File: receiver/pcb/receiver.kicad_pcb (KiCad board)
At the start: 2 copper layers, 39 x 43.2 mm, 23 parts, among them M1 Conn_01x02_Female, M2 Conn_01x02_Female, U1 DRV8870DDA, U2 DRV8870DDA

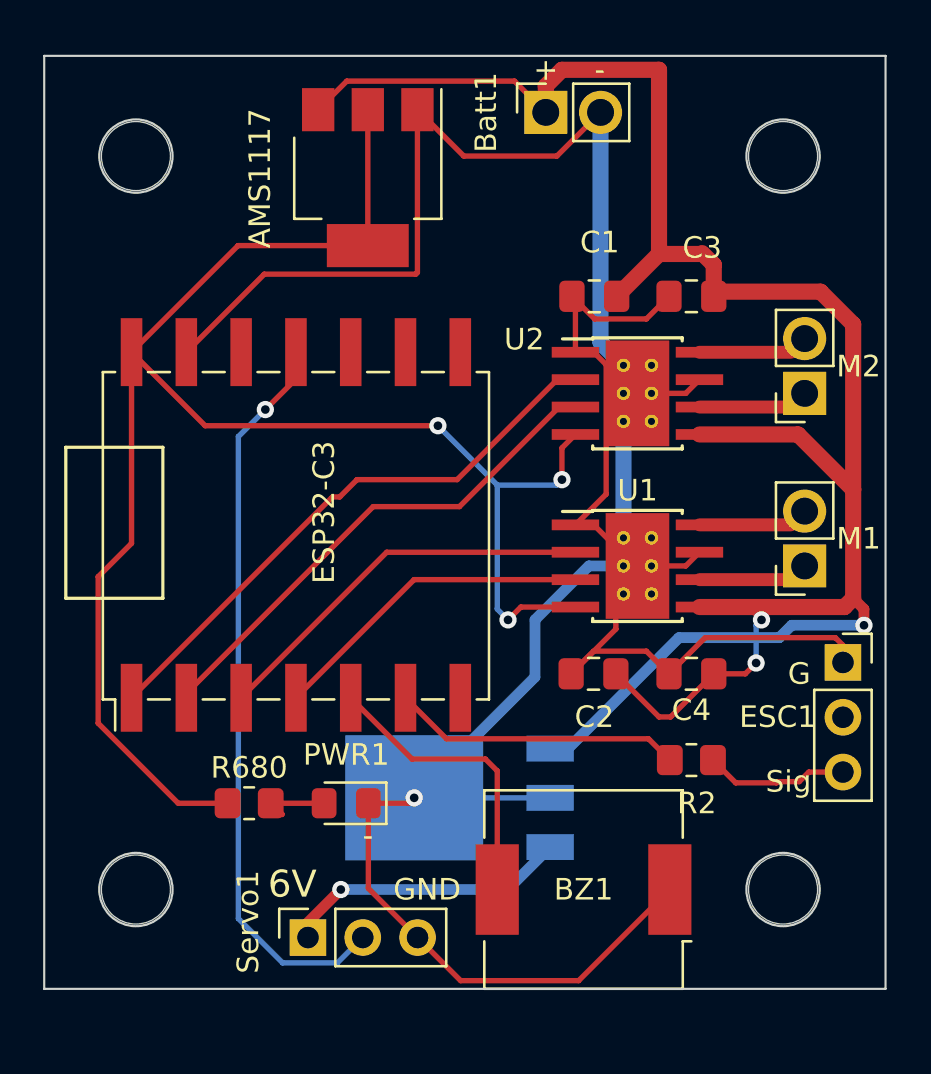
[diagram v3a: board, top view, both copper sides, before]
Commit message: made square pin consistently more positive voltage
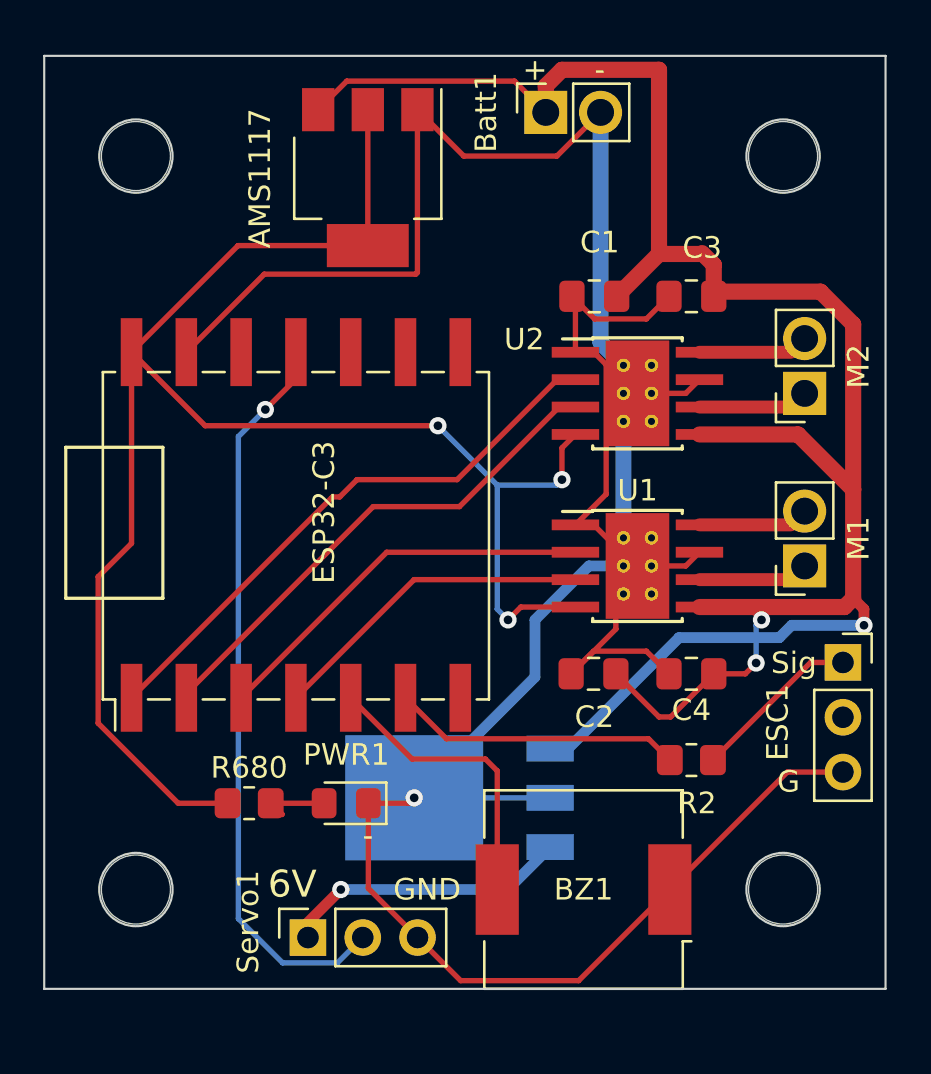
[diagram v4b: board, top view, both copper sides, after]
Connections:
- ESC1 pad 1: GND -> Net-(ESC1-Pad1)
- ESC1 pad 3: Net-(R2-Pad2) -> GND
- R2 pad 2: Net-(R2-Pad2) -> Net-(ESC1-Pad1)
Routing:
- net Net-(ESC1-Pad1): track 0.00 -> 7.90 mm
- net Net-(R2-Pad2): track 6.67 -> 0.00 mm
- net GND: track 140.7 -> 141.3 mm
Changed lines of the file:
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@@
   (net 6 "Net-(M2-Pad1)")
   (net 7 "Net-(M2-Pad2)")
-  (net 8 "Net-(R2-Pad2)")
+  (net 8 "Net-(ESC1-Pad1)")
   (net 9 "Net-(ESP32-C3-Pad19)")
-  (net 10 "Net-(U1-Pad2)")
-  (net 11 "Net-(U1-Pad3)")
+  (net 10 "Net-(ESP32-C3-Pad5)")
+  (net 11 "Net-(ESP32-C3-Pad6)")
   (net 12 "+3V3")
-  (net 13 "Net-(U2-Pad2)")
-  (net 14 "Net-(U2-Pad3)")
+  (net 13 "Net-(ESP32-C3-Pad12)")
+  (net 14 "Net-(ESP32-C3-Pad13)")
   (net 15 "unconnected-(ESP32-C3-Pad20)")
   (net 16 "/spkr")
@@
       (net 12 "+3V3") (pinfunction "3V3") (pintype "power_in"))
     (pad "5" smd rect (at -8.6 -4.34 90) (size 3.15 1) (layers "F.Cu" "F.Paste" "F.Mask")
-      (net 10 "Net-(U1-Pad2)") (pinfunction "GPIO2/ADC1_CH2") (pintype "bidirectional"))
+      (net 10 "Net-(ESP32-C3-Pad5)") (pinfunction "GPIO2/ADC1_CH2") (pintype "bidirectional"))
     (pad "6" smd rect (at -8.6 -1.8 90) (size 3.15 1) (layers "F.Cu" "F.Paste" "F.Mask")
-      (net 11 "Net-(U1-Pad3)") (pinfunction "GPIO3/ADC1_CH3") (pintype "bidirectional"))
+      (net 11 "Net-(ESP32-C3-Pad6)") (pinfunction "GPIO3/ADC1_CH3") (pintype "bidirectional"))
     (pad "12" smd rect (at -8.6 -9.42 90) (size 3.15 1) (layers "F.Cu" "F.Paste" "F.Mask")
-      (net 13 "Net-(U2-Pad2)") (pinfunction "GPIO0/ADC1_CH0/XTAL_32K_P") (pintype "bidirectional"))
+      (net 13 "Net-(ESP32-C3-Pad12)") (pinfunction "GPIO0/ADC1_CH0/XTAL_32K_P") (pintype "bidirectional"))
     (pad "13" smd rect (at -8.6 -6.88 90) (size 3.15 1) (layers "F.Cu" "F.Paste" "F.Mask")
-      (net 14 "Net-(U2-Pad3)") (pinfunction "GPIO1/ADC1_CH1/XTAL_32K_N") (pintype "bidirectional"))
+      (net 14 "Net-(ESP32-C3-Pad13)") (pinfunction "GPIO1/ADC1_CH1/XTAL_32K_N") (pintype "bidirectional"))
     (pad "16" smd rect (at 7.425 -1.8 90) (size 3.15 1) (layers "F.Cu" "F.Paste" "F.Mask")
       (net 19 "/Servo") (pinfunction "GPIO10") (pintype "bidirectional"))
@@
       (net 9 "Net-(ESP32-C3-Pad19)") (pintype "passive"))
     (pad "2" smd roundrect (at 1 0) (size 1.2 1.4) (layers "F.Cu" "F.Paste" "F.Mask") (roundrect_rratio 0.2083333333)
-      (net 8 "Net-(R2-Pad2)") (pintype "passive"))
+      (net 8 "Net-(ESC1-Pad1)") (pintype "passive"))
     (model "${KICAD6_3DMODEL_DIR}/Resistor_SMD.3dshapes/R_0805_2012Metric.wrl"
       (offset (xyz 0 0 0))
@@
     (property "Sheetname" "")
     (attr through_hole)
-    (fp_text reference "ESC1" (at -3.025 2.525) (layer "F.SilkS")
+    (fp_text reference "ESC1" (at -3.025 2.775 90) (layer "F.SilkS")
       (effects (font (size 1 1) (thickness 0.15)))
     )
@@
     (fp_line (start -1.27 6.35) (end -1.27 -1.27) (layer "F.Fab") (width 0.1))
     (pad "1" thru_hole rect (at 0 0) (size 1.7 1.7) (drill 1) (layers *.Cu *.Mask)
-      (net 2 "GND") (pinfunction "Pin_1") (pintype "passive"))
+      (net 8 "Net-(ESC1-Pad1)") (pinfunction "Pin_1") (pintype "passive"))
     (pad "2" thru_hole oval (at 0 2.54) (size 1.7 1.7) (drill 1) (layers *.Cu *.Mask)
       (net 3 "unconnected-(ESC1-Pad2)") (pinfunction "Pin_2") (pintype "passive+no_connect"))
     (pad "3" thru_hole oval (at 0 5.08) (size 1.7 1.7) (drill 1) (layers *.Cu *.Mask)
-      (net 8 "Net-(R2-Pad2)") (pinfunction "Pin_3") (pintype "passive"))
+      (net 2 "GND") (pinfunction "Pin_3") (pintype "passive"))
     (model "${KICAD6_3DMODEL_DIR}/Connector_PinSocket_2.54mm.3dshapes/PinSocket_1x03_P2.54mm_Vertical.wrl"
       (offset (xyz 0 0 0))
@@
     (property "Sheetname" "")
     (attr through_hole)
-    (fp_text reference "M1" (at -2.5 1.27) (layer "F.SilkS")
+    (fp_text reference "M1" (at -2.5 1.27 90) (layer "F.SilkS")
       (effects (font (size 1 1) (thickness 0.15)))
     )
@@
     (property "Sheetname" "")
     (attr through_hole)
-    (fp_text reference "M2" (at -2.5 1.25) (layer "F.SilkS")
+    (fp_text reference "M2" (at -2.5 1.25 90) (layer "F.SilkS")
       (effects (font (size 1 1) (thickness 0.15)))
     )
@@
       (net 2 "GND") (pinfunction "GND") (pintype "power_in"))
     (pad "2" smd rect (at -2.875 -0.635) (size 2.2 0.5) (layers "F.Cu" "F.Paste" "F.Mask")
-      (net 10 "Net-(U1-Pad2)") (pinfunction "IN2") (pintype "input"))
+      (net 10 "Net-(ESP32-C3-Pad5)") (pinfunction "IN2") (pintype "input"))
     (pad "3" smd rect (at -2.875 0.635) (size 2.2 0.5) (layers "F.Cu" "F.Paste" "F.Mask")
-      (net 11 "Net-(U1-Pad3)") (pinfunction "IN1") (pintype "input"))
+      (net 11 "Net-(ESP32-C3-Pad6)") (pinfunction "IN1") (pintype "input"))
     (pad "4" smd rect (at -2.875 1.905) (size 2.2 0.5) (layers "F.Cu" "F.Paste" "F.Mask")
       (net 12 "+3V3") (pinfunction "VREF") (pintype "input"))
@@
       (net 2 "GND") (pinfunction "GND") (pintype "power_in"))
     (pad "2" smd rect (at -2.875 -0.635) (size 2.2 0.5) (layers "F.Cu" "F.Paste" "F.Mask")
-      (net 13 "Net-(U2-Pad2)") (pinfunction "IN2") (pintype "input"))
+      (net 13 "Net-(ESP32-C3-Pad12)") (pinfunction "IN2") (pintype "input"))
     (pad "3" smd rect (at -2.875 0.635) (size 2.2 0.5) (layers "F.Cu" "F.Paste" "F.Mask")
-      (net 14 "Net-(U2-Pad3)") (pinfunction "IN1") (pintype "input"))
+      (net 14 "Net-(ESP32-C3-Pad13)") (pinfunction "IN1") (pintype "input"))
     (pad "4" smd rect (at -2.875 1.905) (size 2.2 0.5) (layers "F.Cu" "F.Paste" "F.Mask")
       (net 12 "+3V3") (pinfunction "VREF") (pintype "input"))
@@
     (effects (font (size 1 1) (thickness 0.15)))
   )
-  (gr_text "G" (at 181.5 105) (layer "F.SilkS")
+  (gr_text "G" (at 181 110) (layer "F.SilkS")
     (effects (font (size 1 1) (thickness 0.15)))
   )
-  (gr_text "+" (at 169.75 77) (layer "F.SilkS")
+  (gr_text "+" (at 169.25 77) (layer "F.SilkS")
     (effects (font (size 1 1) (thickness 0.15)))
   )
-  (gr_text "Sig" (at 181 110) (layer "F.SilkS")
+  (gr_text "Sig" (at 181.25 104.5) (layer "F.SilkS")
     (effects (font (size 1 1) (thickness 0.15)))
   )
@@
   (segment (start 173 102.925) (end 170.925 105) (width 0.25) (layer "F.Cu") (net 2))
   (segment (start 163.805 117.225) (end 165.805 119.225) (width 0.25) (layer "F.Cu") (net 2))
-  (segment (start 183.174511 103.325489) (end 183.525 103.675978) (width 0.25) (layer "F.Cu") (net 2))
   (segment (start 161.525 111) (end 163.4 111) (width 0.25) (layer "F.Cu") (net 2))
   (segment (start 163.8 86.399022) (end 163.8 78.85) (width 0.25) (layer "F.Cu") (net 2))
   (segment (start 171.975 98.095) (end 173 99.12) (width 0.25) (layer "F.Cu") (net 2))
   (segment (start 171.97452 103.95048) (end 170.925 105) (width 0.25) (layer "F.Cu") (net 2))
+  (segment (start 183.525 109.555) (end 180.945 109.555) (width 0.25) (layer "F.Cu") (net 2))
   (segment (start 165.805 119.225) (end 171.275 119.225) (width 0.25) (layer "F.Cu") (net 2))
   (segment (start 174.65 92) (end 176.24 92) (width 0.25) (layer "F.Cu") (net 2))
@@
   (segment (start 156.700489 86.474511) (end 163.724511 86.474511) (width 0.25) (layer "F.Cu") (net 2))
   (segment (start 172.549511 90.669511) (end 172.549511 96.670489) (width 0.25) (layer "F.Cu") (net 2))
+  (segment (start 180.945 109.555) (end 175.5 115) (width 0.25) (layer "F.Cu") (net 2))
   (segment (start 170.9625 87.5) (end 171.125 87.6625) (width 0.25) (layer "F.Cu") (net 2))
   (segment (start 163.8 78.85) (end 165.95 81) (width 0.25) (layer "F.Cu") (net 2))
   (segment (start 163.724511 86.474511) (end 163.8 86.399022) (width 0.25) (layer "F.Cu") (net 2))
-  (segment (start 177.137011 103.325489) (end 175.4625 105) (width 0.25) (layer "F.Cu") (net 2))
   (segment (start 173 99.12) (end 173 102.925) (width 0.25) (layer "F.Cu") (net 2))
   (segment (start 165.95 81) (end 170.265 81) (width 0.25) (layer "F.Cu") (net 2))
   (segment (start 153.0875 90.0875) (end 156.700489 86.474511) (width 0.25) (layer "F.Cu") (net 2))
-  (segment (start 183.174511 103.325489) (end 177.137011 103.325489) (width 0.25) (layer "F.Cu") (net 2))
   (segment (start 171.975 90.095) (end 171.125 90.095) (width 0.25) (layer "F.Cu") (net 2))
   (segment (start 174.41298 103.95048) (end 171.97452 103.95048) (width 0.25) (layer "F.Cu") (net 2))
@@
   (segment (start 174.65 100) (end 176.24 100) (width 0.25) (layer "F.Cu") (net 2))
   (segment (start 175.4625 87.5) (end 174.41298 88.54952) (width 0.25) (layer "F.Cu") (net 2))
-  (segment (start 183.525 103.675978) (end 183.525 104.475) (width 0.25) (layer "F.Cu") (net 2))
   (segment (start 175.5 115) (end 171.275 119.225) (width 0.25) (layer "F.Cu") (net 2))
   (segment (start 171.975 90.095) (end 172.549511 90.669511) (width 0.25) (layer "F.Cu") (net 2))
@@
   (segment (start 176.875 90.095) (end 181.115 90.095) (width 0.6) (layer "F.Cu") (net 7))
   (segment (start 181.115 90.095) (end 181.75 89.46) (width 0.25) (layer "F.Cu") (net 7))
-  (segment (start 178.555 110.055) (end 180.445 110.055) (width 0.25) (layer "F.Cu") (net 8))
-  (segment (start 177.5 109) (end 178.555 110.055) (width 0.25) (layer "F.Cu") (net 8))
-  (segment (start 180.5 110) (end 181.5 110) (width 0.25) (layer "F.Cu") (net 8))
-  (segment (start 181.945 109.555) (end 183.525 109.555) (width 0.25) (layer "F.Cu") (net 8))
-  (segment (start 181.5 110) (end 181.945 109.555) (width 0.25) (layer "F.Cu") (net 8))
-  (segment (start 180.445 110.055) (end 180.5 110) (width 0.25) (layer "F.Cu") (net 8))
+  (segment (start 182.025 104.475) (end 183.525 104.475) (width 0.25) (layer "F.Cu") (net 8))
+  (segment (start 177.5 109) (end 182.025 104.475) (width 0.25) (layer "F.Cu") (net 8))
   (segment (start 174.512011 108.012011) (end 175.5 109) (width 0.25) (layer "F.Cu") (net 9))
   (segment (start 165.147011 108.012011) (end 174.512011 108.012011) (width 0.25) (layer "F.Cu") (net 9))
